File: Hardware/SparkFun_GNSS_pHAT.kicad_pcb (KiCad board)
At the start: 4 copper layers, 65 x 56.8 mm, 116 parts, among them J1 Raspberry_Pi_2x20_SMD_Passthr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, J2 Conn_02x10, J3 U.FL, J4 Conn_02x10, J5 microSD_Friction, J6 USB_C_Receptacle, J7 SMA_Edge, J8 Qwiic_Vertical, J9 Conn_01x05, U1 CAT24C512WI-GT3, U2 AP7361C-3.3V, U3 STLQ015-3.3

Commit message: pHAT updated after review
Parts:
- removed JP16, JP17, JP18, JP19, JP20, JP21: ~, SparkFun-Jumper:Jumper_2_NC_Trace
- added JP24: ~, SparkFun-Jumper:Jumper_2_NC_Trace, B.Cu at (144.3, 77.5)
- added JP25: ~, SparkFun-Jumper:Jumper_2_NC_Trace, B.Cu at (149.4, 77.5)
- added PPS1.1: ~, SparkFun-Jumper:Jumper_2_NC_Trace, F.Cu at (168.5, 97.5)
- added PVT.1: ~, SparkFun-Jumper:Jumper_2_NC_Trace, F.Cu at (168.5, 101.6)
- added PWR.1: ~, SparkFun-Jumper:Jumper_2_NC_Trace, F.Cu at (168.5, 95.5)
- added RTK.1: ~, SparkFun-Jumper:Jumper_2_NC_Trace, F.Cu at (168.5, 99.6)
- added TP1: 1.25mm, SparkFun-Connector:TestPoint-1.25mm, B.Cu at (157.0, 74.8)
- added TP10: 1.25mm, SparkFun-Connector:TestPoint-1.25mm, B.Cu at (149.4, 74.8)
- added TP11: 1.25mm, SparkFun-Connector:TestPoint-1.25mm, B.Cu at (146.8, 74.8)
- added TP12: 1.25mm, SparkFun-Connector:TestPoint-1.25mm, B.Cu at (151.9, 74.8)
- added TP13: 1.25mm, SparkFun-Connector:TestPoint-1.25mm, B.Cu at (162.1, 69.1)
- added TP14: 1.25mm, SparkFun-Connector:TestPoint-1.25mm, B.Cu at (164.6, 74.8)
- added TP15: 1.25mm, SparkFun-Connector:TestPoint-1.25mm, B.Cu at (131.6, 69.1)
- added TP16: 1.25mm, SparkFun-Connector:TestPoint-1.25mm, B.Cu at (134.1, 69.1)
- added TP17: 1.25mm, SparkFun-Connector:TestPoint-1.25mm, B.Cu at (141.7, 74.8)
- added TP18: 1.25mm, SparkFun-Connector:TestPoint-1.25mm, B.Cu at (141.7, 69.1)
- added TP19: 1.25mm, SparkFun-Connector:TestPoint-1.25mm, B.Cu at (144.3, 69.1)
- added TP2: 1.25mm, SparkFun-Connector:TestPoint-1.25mm, B.Cu at (157.0, 69.1)
- added TP20: 1.25mm, SparkFun-Connector:TestPoint-1.25mm, B.Cu at (149.4, 69.1)
- added TP21: 1.25mm, SparkFun-Connector:TestPoint-1.25mm, B.Cu at (136.6, 121.6)
- added TP22: 1.25mm, SparkFun-Connector:TestPoint-1.25mm, B.Cu at (124.0, 69.1)
- added TP23: 1.25mm, SparkFun-Connector:TestPoint-1.25mm, B.Cu at (124.0, 74.8)
- added TP24: 1.25mm, SparkFun-Connector:TestPoint-1.25mm, B.Cu at (146.6, 121.6)
- added TP25: 1.25mm, SparkFun-Connector:TestPoint-1.25mm, B.Cu at (148.6, 121.6)
- added TP26: 1.25mm, SparkFun-Connector:TestPoint-1.25mm, B.Cu at (150.6, 121.6)
- added TP27: 1.25mm, SparkFun-Connector:TestPoint-1.25mm, B.Cu at (146.6, 117.3)
- added TP28: 1.25mm, SparkFun-Connector:TestPoint-1.25mm, B.Cu at (144.6, 117.3)
- added TP29: 1.25mm, SparkFun-Connector:TestPoint-1.25mm, B.Cu at (142.6, 117.3)
- added TP3: 1.25mm, SparkFun-Connector:TestPoint-1.25mm, B.Cu at (126.5, 74.8)
- added TP30: 1.25mm, SparkFun-Connector:TestPoint-1.25mm, B.Cu at (140.6, 117.3)
- added TP31: 1.25mm, SparkFun-Connector:TestPoint-1.25mm, B.Cu at (129.0, 69.1)
- added TP4: 1.25mm, SparkFun-Connector:TestPoint-1.25mm, B.Cu at (129.0, 74.8)
- added TP5: 1.25mm, SparkFun-Connector:TestPoint-1.25mm, B.Cu at (131.6, 74.8)
- added TP6: 1.25mm, SparkFun-Connector:TestPoint-1.25mm, B.Cu at (159.5, 74.8)
- added TP7: 1.25mm, SparkFun-Connector:TestPoint-1.25mm, B.Cu at (162.1, 74.8)
- added TP8: 1.25mm, SparkFun-Connector:TestPoint-1.25mm, B.Cu at (154.4, 69.1)
- added TP9: 1.25mm, SparkFun-Connector:TestPoint-1.25mm, B.Cu at (151.9, 69.1)
- JP12, JP15, JP23: moved to B.Cu
- JP13, JP4, JP5, JP9: moved to F.Cu
- R14: value 1k -> 4.7k
- U3: value STLQ015-3.3 -> RT9080-3.3
- moved JP22 33.5 mm to (141.7, 77.5), turned to 90 degrees
- moved JP23 32.3 mm to (141.7, 77.5), turned to 90 degrees
- moved JP5 25.4 mm to (159.5, 77.5), turned to -90 degrees
- moved JP14 20.3 mm to (131.6, 77.5), turned to 90 degrees
- moved JP6 20.3 mm to (162.1, 77.5), turned to -90 degrees
- moved JP10 15.2 mm to (146.8, 77.6)
- moved JP15 15.2 mm to (134.1, 77.5), turned to 90 degrees
- moved JP7 12.7 mm to (154.4, 77.5), turned to -90 degrees
- moved JP13 10.2 mm to (164.6, 77.5)
- moved JP11 7.62 mm to (151.9, 77.5)
- moved JP8 7.62 mm to (151.9, 77.5), turned to -90 degrees
- turned JP4 to -90 degrees
- turned JP9 to -90 degrees
- turned R14 to 0 degrees
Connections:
- JP10 pad 1: Net-(J1-GCLK0/GPIO4) -> Net-(J1-PICO0/GPIO10)
- JP10 pad 2: RXD3 -> RTS2
- JP11 pad 1: Net-(J1-GCLK1/GPIO5) -> Net-(J1-SCLK0/GPIO11)
- JP11 pad 2: TXD3 -> CTS2
- JP12 pad 1: Net-(J1-GCLK2/GPIO6) -> Net-(J1-PWM0/GPIO12)
- JP12 pad 2: RTS3 -> RXD4
- JP13 pad 1: Net-(J1-~{CE1}/GPIO7) -> Net-(J1-PWM1/GPIO13)
- JP13 pad 2: CTS3 -> TXD4
- JP14 pad 1: Net-(J1-~{CE0}/GPIO8) -> RXD1
- JP14 pad 2: RXD2 -> Net-(J1-GPIO14/TXD)
- JP15 pad 1: Net-(J1-POCI0/GPIO9) -> TXD1
- JP15 pad 2: TXD2 -> Net-(J1-GPIO15/RXD)
- JP22 pad 2: Net-(JP22-B) -> Net-(J1-GPIO22)
- JP23 pad 1: Net-(JP23-A) -> PPS2
- JP23 pad 2: 3.3V -> Net-(J1-GPIO23)
- JP4 pad 1: RXD1 -> Net-(J1-GCLK0/GPIO4)
- JP4 pad 2: Net-(J1-GPIO14/TXD) -> RXD3
- JP5 pad 1: TXD1 -> Net-(J1-GCLK1/GPIO5)
- JP5 pad 2: Net-(J1-GPIO15/RXD) -> TXD3
- JP6 pad 1: PPS1 -> Net-(J1-GCLK2/GPIO6)
- JP6 pad 2: Net-(J1-GPIO22) -> RTS3
- JP7 pad 1: PPS2 -> Net-(J1-~{CE1}/GPIO7)
- JP7 pad 2: Net-(J1-GPIO23) -> CTS3
- JP8 pad 1: EVENTA -> Net-(J1-~{CE0}/GPIO8)
- JP8 pad 2: Net-(J1-GPIO24) -> RXD2
- JP9 pad 1: EVENTB -> Net-(J1-POCI0/GPIO9)
- JP9 pad 2: Net-(J1-GPIO25) -> TXD2
- R13 pad 2: Net-(JP22-B) -> Net-(PPS1.1-B)
- R14 pad 1: Net-(D6-A) -> Net-(PWR.1-A)
- R14 pad 2: Net-(JP23-A) -> Net-(D6-A)
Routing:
- net D-: track 43.7 -> 41.4 mm
- net Net-(PWR.1-A): track 0.00 -> 1.70 mm
- net Net-(PPS1.1-B): track 0.00 -> 1.70 mm
- net Net-(JP23-A): track 1.70 -> 0.00 mm
- net Net-(JP22-B): track 1.70 -> 0.00 mm
- net Pi_3V3: track 63.8 -> 65.2 mm, vias 4 -> 5
- net 5V: track 97.2 -> 96.0 mm, vias 6 -> 7
- net 3.3V: track 55.2 -> 53.9 mm
- net VBACKUP: track 18.6 -> 18.5 mm, vias 0 -> 1
- net SDA: vias 4 -> 5
- net SCL: vias 4 -> 5
- net ID_SD: vias 2 -> 3
- net Net-(J1-SCLK0/GPIO11): track 2.13 -> 2.16 mm, vias 0 -> 1
- net Net-(J1-PWM1/GPIO13): track 2.13 -> 2.16 mm, vias 0 -> 1
- net Net-(J1-POCI0/GPIO9): track 2.13 -> 2.16 mm, vias 0 -> 1
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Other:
- board text removed: "1"
- board text removed: "2"
- board text removed: "3"
- board text removed: "4"

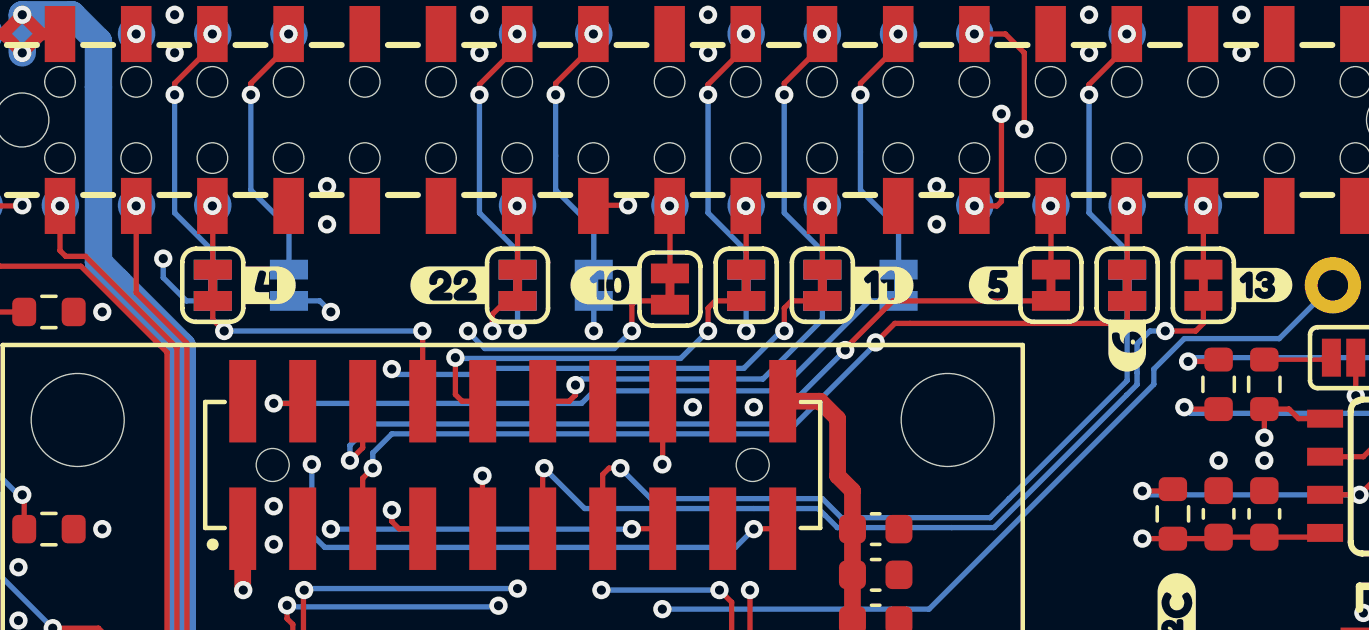
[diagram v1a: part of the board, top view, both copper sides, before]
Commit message: Update standoffs. Change panel to 2x2
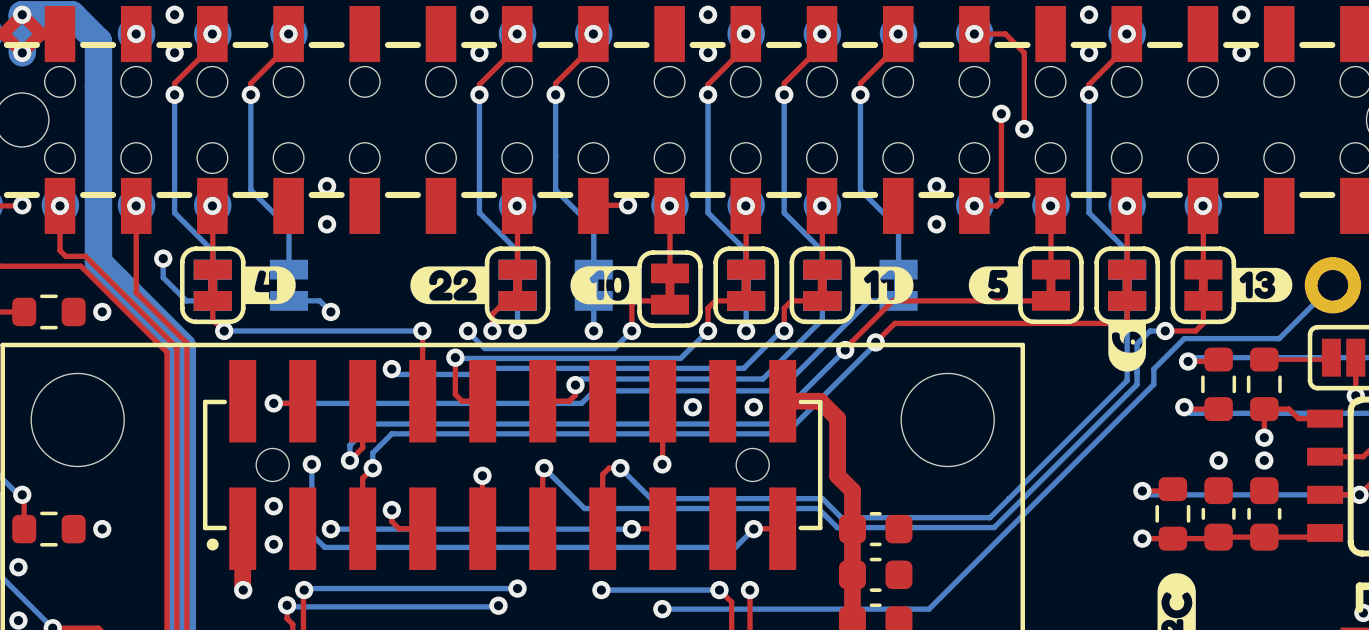
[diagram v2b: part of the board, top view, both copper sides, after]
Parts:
- J8: footprint SparkFun-Connector:JST_SMD_1.0mm-4_Vertical -> SparkFun-Connector:JST_SMD_1.0mm-4_Vertical_Black
- ST5, ST6, ST7, ST8: footprint SparkFun-Hardware:Standoff_Raspberry-Pi_HAT+ -> SparkFun-Hardware:Standoff_Hole-2.75mm_Clearance-1.625mm

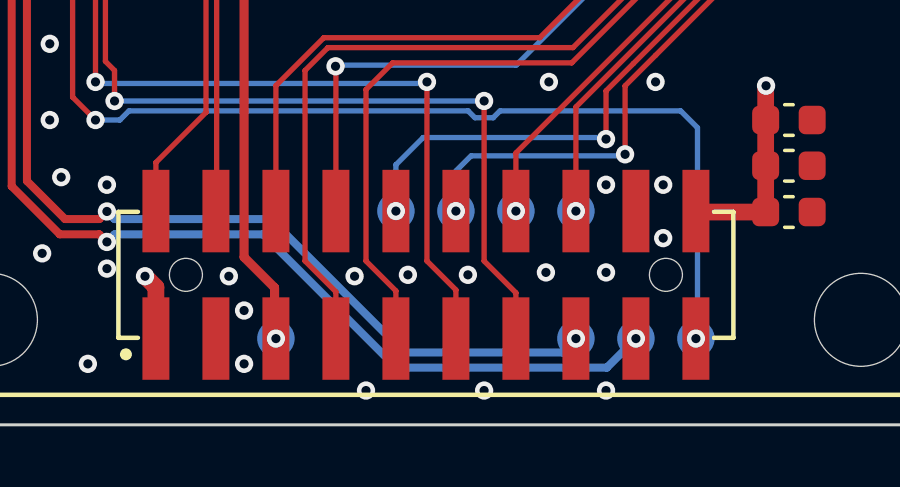
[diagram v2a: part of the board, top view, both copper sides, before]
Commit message: Update RPi passthrough connector PROD_ID
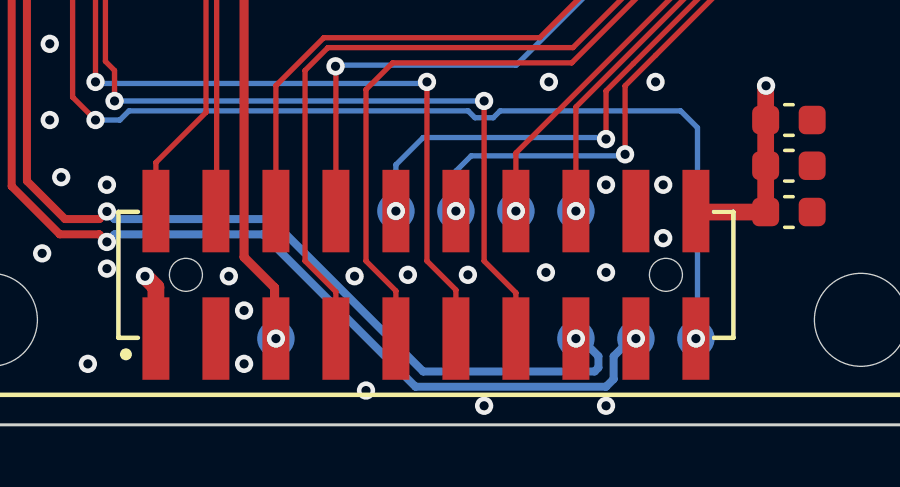
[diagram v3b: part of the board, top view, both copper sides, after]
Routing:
- net D-: track 41.4 -> 43.0 mm
- net D+: track 43.8 -> 44.7 mm
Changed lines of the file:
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@@
 		(sheetfile "SparkFun_GNSS_pHAT.kicad_sch")
 		(attr exclude_from_pos_files exclude_from_bom)
-		(fp_text user "Released under the Creative Commons Attribution Share-Alike 4.0 License"
-			(at 0 -1.27 0)
+		(fp_text user " https://creativecommons.org/licenses/by-sa/4.0/"
+			(at 0 1.27 0)
 			(layer "F.Fab")
 			(effects
@@
 			)
 		)
-		(fp_text user " https://creativecommons.org/licenses/by-sa/4.0/"
-			(at 0 1.27 0)
+		(fp_text user "Released under the Creative Commons Attribution Share-Alike 4.0 License"
+			(at 0 -1.27 0)
 			(layer "F.Fab")
 			(effects
@@
 		)
 		(group ""
-			(members "208d331e-603e-4798-9605-8ce98b2dda71" "4d35aadc-6067-4cd8-9f54-19d21914c07a"
-				"554aca9f-8835-49f6-a8c4-e0c59e9eadee" "56045dfe-0de0-4c43-b423-fb0fe613e70a"
-				"63c2d6c9-2865-43b3-a578-cd9afce7216d" "67700d02-5702-42a4-a4cb-767054e0173c"
-				"c7e1cff3-6d48-480f-a3c0-eb8e5762caa6" "e4f26129-ca9e-4349-b8fd-cc8dff7cc6d8"
-				"f8bca8ad-7a65-40aa-a094-1b4078950d2e"
+			(members "09b43eef-63d2-4db9-a3ea-c691a665bdfd" "0faf9cef-ba9f-453b-8482-ddee09a844f1"
+				"20f6e810-b0bc-4869-9717-5ea4d64cfe25" "2c15f9de-2972-4b4c-878a-d30ac9a3ac52"
+				"3ca2f8b5-1f87-4ab3-943a-81be2a9ee665" "6499b889-840a-4611-b178-e17d687c1621"
+				"8ecbebd4-4dfe-45a0-a7d7-0fec8669c633" "98d16e61-6c96-43c8-b1ec-94c5096543f3"
+				"c624862e-9317-4f0b-be26-5d4e3f83d271"
 			)
 		)
@@
 			)
 		)
-		(property "Datasheet" "https://cdn.harwin.com/pdfs/M20-781.pdf"
+		(property "Datasheet" "http://www.4uconnector.com/online/object/4udrawing/10956.pdf"
 			(at 0 26.924 90)
 			(layer "F.Fab")
@@
 			)
 		)
-		(property "PROD_ID" "CONN-24972"
+		(property "PROD_ID" "CONN-13790"
 			(at 0 0 90)
 			(unlocked yes)
@@
 			(layer "User.1")
 		)
-		(fp_text user "ETHERNET"
-			(at -42.164 42.164 180)
+		(fp_text user "DISPLAY"
+			(at -23.368 -29.464 90)
 			(unlocked yes)
 			(layer "User.1")
@@
 			)
 		)
-		(fp_text user "USB"
-			(at -5.08 44.704 180)
+		(fp_text user "ETHERNET"
+			(at -42.164 42.164 180)
 			(unlocked yes)
 			(layer "User.1")
@@
 			)
 		)
-		(fp_text user "HDMI"
-			(at -47.244 0 180)
+		(fp_text user "USB"
+			(at -5.08 44.704 180)
 			(unlocked yes)
 			(layer "User.1")
@@
 			)
 		)
-		(fp_text user "USB"
-			(at -49.784 -21.844 180)
+		(fp_text user "CAMERA"
+			(at -40.132 13.208 90)
 			(unlocked yes)
 			(layer "User.1")
@@
 			)
 		)
-		(fp_text user "USB"
-			(at -23.368 44.704 180)
+		(fp_text user "HDMI"
+			(at -47.244 0 180)
 			(unlocked yes)
 			(layer "User.1")
@@
 			)
 		)
-		(fp_text user "DISPLAY"
-			(at -23.368 -29.464 90)
+		(fp_text user "USB"
+			(at -49.784 -21.844 180)
 			(unlocked yes)
 			(layer "User.1")
@@
 			)
 		)
-		(fp_text user "CAMERA"
-			(at -40.132 13.208 90)
+		(fp_text user "USB"
+			(at -23.368 44.704 180)
 			(unlocked yes)
 			(layer "User.1")
@@
 		)
 		(group ""
-			(members "2b2247ff-169e-44fe-878f-48290a6f27bb" "3cf394e7-bc0a-4acc-8b3c-5bad4c4b72e5"
-				"5b116b63-4233-4944-91f9-8a46e011205b" "5e53450b-572a-4231-a8d7-f9b5d60b6b2d"
-				"7806ff3a-29e5-4379-8242-cb94f85f340b" "c01d3b03-254f-4b04-9f19-a438535b29be"
-				"ce4a8bc1-6bd0-44a5-ae5d-41c6870b168a" "de87bab4-d622-46d4-972f-89d9a37a7fe1"
-				"fe7092fd-1d88-44ad-bd71-63cab43ac03b"
+			(members "2a0aa500-6c62-47e4-8961-df437ecfe88b" "3279c6f7-7ab2-40c2-bd90-80dce5a715f6"
+				"49d9a73c-c611-4147-b1d0-3a9d1e367e4a" "6b9640fe-41c9-4c9f-8844-8ac6ea1592cd"
+				"83acd65c-4fab-4e56-a83d-26c0ab1e8a22" "9629bc94-895d-4f93-8967-b9fa32181951"
+				"aafa1818-d2fd-48fd-8eb1-33a9d1ebab6c" "c60d2adf-d8b5-4b33-ae35-e9f27976e5ff"
+				"ee630ec0-0375-4431-b008-7f6dd9937181"
 			)
 		)
@@
 	)
 	(via
-		(at 143.51 123.317)
+		(at 143.51 123.825)
 		(size 0.6096)
 		(drill 0.3048)
@@
 	)
 	(via
-		(at 147.574 123.317)
+		(at 147.574 123.825)
 		(size 0.6096)
 		(drill 0.3048)
@@
 	)
 	(segment
-		(start 148.524 121.539)
-		(end 148.57 121.585)
-		(width 0.3302)
-		(layer "F.Cu")
-		(net 27)
-	)
-	(segment
 		(start 125.984 98.298)
 		(end 125.838 98.152)
@@
 	)
 	(segment
-		(start 147.6 122.555)
+		(start 147.828 122.936)
+		(end 147.828 122.174)
+		(width 0.2667)
+		(layer "B.Cu")
+		(net 27)
+	)
+	(segment
+		(start 130.937 118.364)
+		(end 131.191 118.11)
+		(width 0.2667)
+		(layer "B.Cu")
+		(net 27)
+	)
+	(segment
+		(start 148.417 121.585)
 		(end 148.57 121.585)
 		(width 0.2667)
@@
 	)
 	(segment
-		(start 131.191 118.11)
-		(end 136.144 118.11)
+		(start 136.144 118.11)
+		(end 141.224 123.19)
 		(width 0.2667)
 		(layer "B.Cu")
@@
 	)
 	(segment
-		(start 130.937 118.364)
-		(end 131.191 118.11)
+		(start 141.224 123.19)
+		(end 147.574 123.19)
 		(width 0.2667)
 		(layer "B.Cu")
@@
 	)
 	(segment
-		(start 140.589 122.555)
-		(end 147.6 122.555)
+		(start 147.828 122.174)
+		(end 148.417 121.585)
 		(width 0.2667)
 		(layer "B.Cu")
@@
 	)
 	(segment
-		(start 136.144 118.11)
-		(end 140.589 122.555)
+		(start 131.191 118.11)
+		(end 136.144 118.11)
+		(width 0.2667)
+		(layer "B.Cu")
+		(net 27)
+	)
+	(segment
+		(start 147.574 123.19)
+		(end 147.828 122.936)
 		(width 0.2667)
 		(layer "B.Cu")
@@
 	)
 	(segment
-		(start 146.57 120.904)
-		(end 146.57 121.585)
-		(width 0.3302)
-		(layer "F.Cu")
-		(net 32)
-	)
-	(segment
 		(start 128.27 100.584)
 		(end 126.492 98.806)
@@
 	(segment
 		(start 136.398 117.602)
-		(end 140.843 122.047)
+		(end 141.478 122.682)
 		(width 0.2667)
 		(layer "B.Cu")
@@
 	)
 	(segment
-		(start 146.108 122.047)
-		(end 146.57 121.585)
+		(start 147.193 122.682)
+		(end 147.32 122.555)
+		(width 0.2667)
+		(layer "B.Cu")
+		(net 32)
+	)
+	(segment
+		(start 147.32 122.555)
+		(end 147.32 122.174)
 		(width 0.2667)
 		(layer "B.Cu")
@@
 	)
 	(segment
-		(start 140.843 122.047)
-		(end 146.108 122.047)
+		(start 147.32 122.174)
+		(end 146.731 121.585)
 		(width 0.2667)
 		(layer "B.Cu")
@@
 		(width 0.2667)
 		(layer "B.Cu")
+		(net 32)
+	)
+	(segment
+		(start 141.478 122.682)
+		(end 147.193 122.682)
+		(width 0.2667)
+		(layer "B.Cu")
+		(net 32)
+	)
+	(segment
+		(start 146.731 121.585)
+		(end 146.57 121.585)
+		(width 0.2667)
+		(layer "B.Cu")

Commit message: Change I2C pull-ups to 3.9K RES-08701
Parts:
- R1, R2, R4, R5: value 3.6k -> 3.9k
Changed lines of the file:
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@@
 			)
 		)
-		(property "Value" "3.6k"
+		(property "Value" "3.9k"
 			(at 0 1.43 180)
 			(layer "F.Fab")
@@
 			)
 		)
-		(property "PROD_ID" "RES-08417"
+		(property "PROD_ID" "RES-08701"
 			(at 0 0 180)
 			(unlocked yes)
@@
 		(fp_arc
 			(start 4.7948 29.512)
-			(mid 3.88034 31.668726)
+			(mid 3.880341 31.668725)
 			(end 1.6948 32.512)
 			(stroke
@@
 			)
 		)
-		(property "Value" "3.6k"
+		(property "Value" "3.9k"
 			(at 0 1.43 180)
 			(layer "F.Fab")
@@
 			)
 		)
-		(property "PROD_ID" "RES-08417"
+		(property "PROD_ID" "RES-08701"
 			(at 0 0 180)
 			(unlocked yes)
@@
 			)
 		)
-		(property "Value" "3.6k"
+		(property "Value" "3.9k"
 			(at 0 1.43 90)
 			(layer "F.Fab")
@@
 			)
 		)
-		(property "PROD_ID" "RES-08417"
+		(property "PROD_ID" "RES-08701"
 			(at 0 0 90)
 			(unlocked yes)
@@
 			)
 		)
-		(property "Value" "3.6k"
+		(property "Value" "3.9k"
 			(at 0 1.43 90)
 			(layer "F.Fab")
@@
 			)
 		)
-		(property "PROD_ID" "RES-08417"
+		(property "PROD_ID" "RES-08701"
 			(at 0 0 90)
 			(unlocked yes)
@@
 		(fp_arc
 			(start 1.5653 -2.590777)
-			(mid 1.834722 -2.479216)
+			(mid 1.834725 -2.479217)
 			(end 1.9463 -2.2098)
 			(stroke
@@
 		(fp_arc
 			(start 0.762 -1.016)
-			(mid 1.08529 -0.88209)
+			(mid 1.085289 -0.882089)
 			(end 1.2192 -0.5588)
 			(stroke
@@
 		(fp_arc
 			(start 0.762 -1.016)
-			(mid 1.08529 -0.88209)
+			(mid 1.085289 -0.882089)
 			(end 1.2192 -0.5588)
 			(stroke
@@
 		(fp_arc
 			(start 0.762 -1.016)
-			(mid 1.08529 -0.88209)
+			(mid 1.085289 -0.882089)
 			(end 1.2192 -0.5588)
 			(stroke
@@
 		(fp_arc
 			(start 0.762 -1.016)
-			(mid 1.08529 -0.88209)
+			(mid 1.085289 -0.882089)
 			(end 1.2192 -0.5588)
 			(stroke
@@
 		(fp_arc
 			(start 0.762 -1.016)
-			(mid 1.08529 -0.88209)
+			(mid 1.085289 -0.882089)
 			(end 1.2192 -0.5588)
 			(stroke
@@
 		(fp_arc
 			(start 0.762 -1.016)
-			(mid 1.08529 -0.88209)
+			(mid 1.085289 -0.882089)
 			(end 1.2192 -0.5588)
 			(stroke
@@
 		(fp_arc
 			(start 0.762 -1.016)
-			(mid 1.08529 -0.88209)
+			(mid 1.085289 -0.882089)
 			(end 1.2192 -0.5588)
 			(stroke
@@
 		(fp_arc
 			(start 0.762 -1.016)
-			(mid 1.08529 -0.88209)
+			(mid 1.085289 -0.882089)
 			(end 1.2192 -0.5588)
 			(stroke
@@
 		(fp_arc
 			(start 0.762 -1.016)
-			(mid 1.08529 -0.88209)
+			(mid 1.085289 -0.882089)
 			(end 1.2192 -0.5588)
 			(stroke
